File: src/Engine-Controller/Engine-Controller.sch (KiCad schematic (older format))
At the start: 14 parts, among them J1 Jumper_NO, U1 STM32H750VBTx

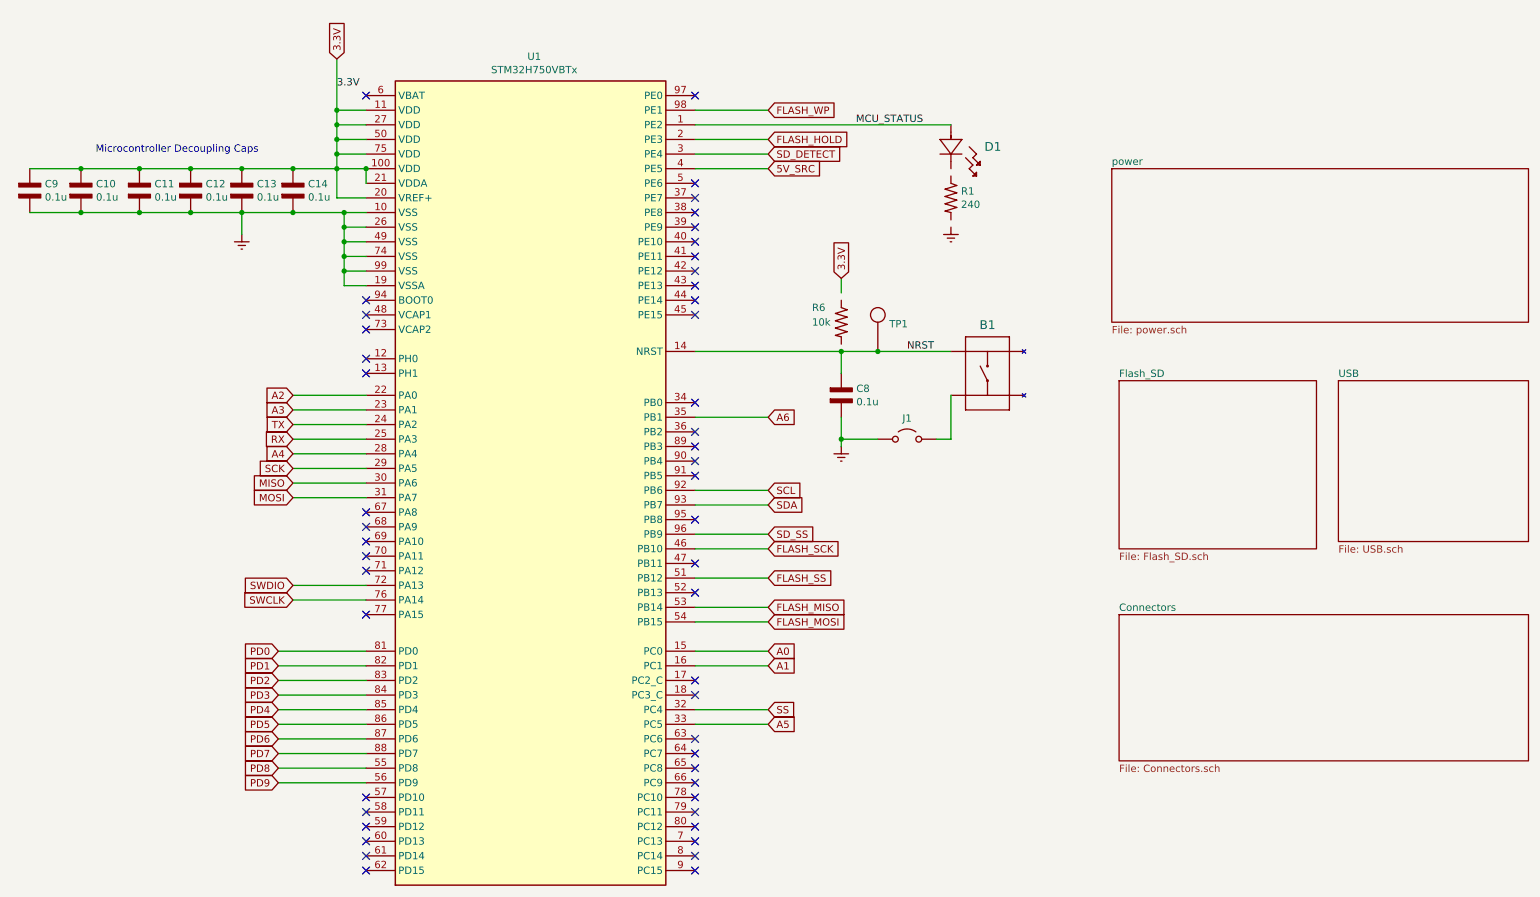
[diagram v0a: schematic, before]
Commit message: Added Ignition System to lib and schematic
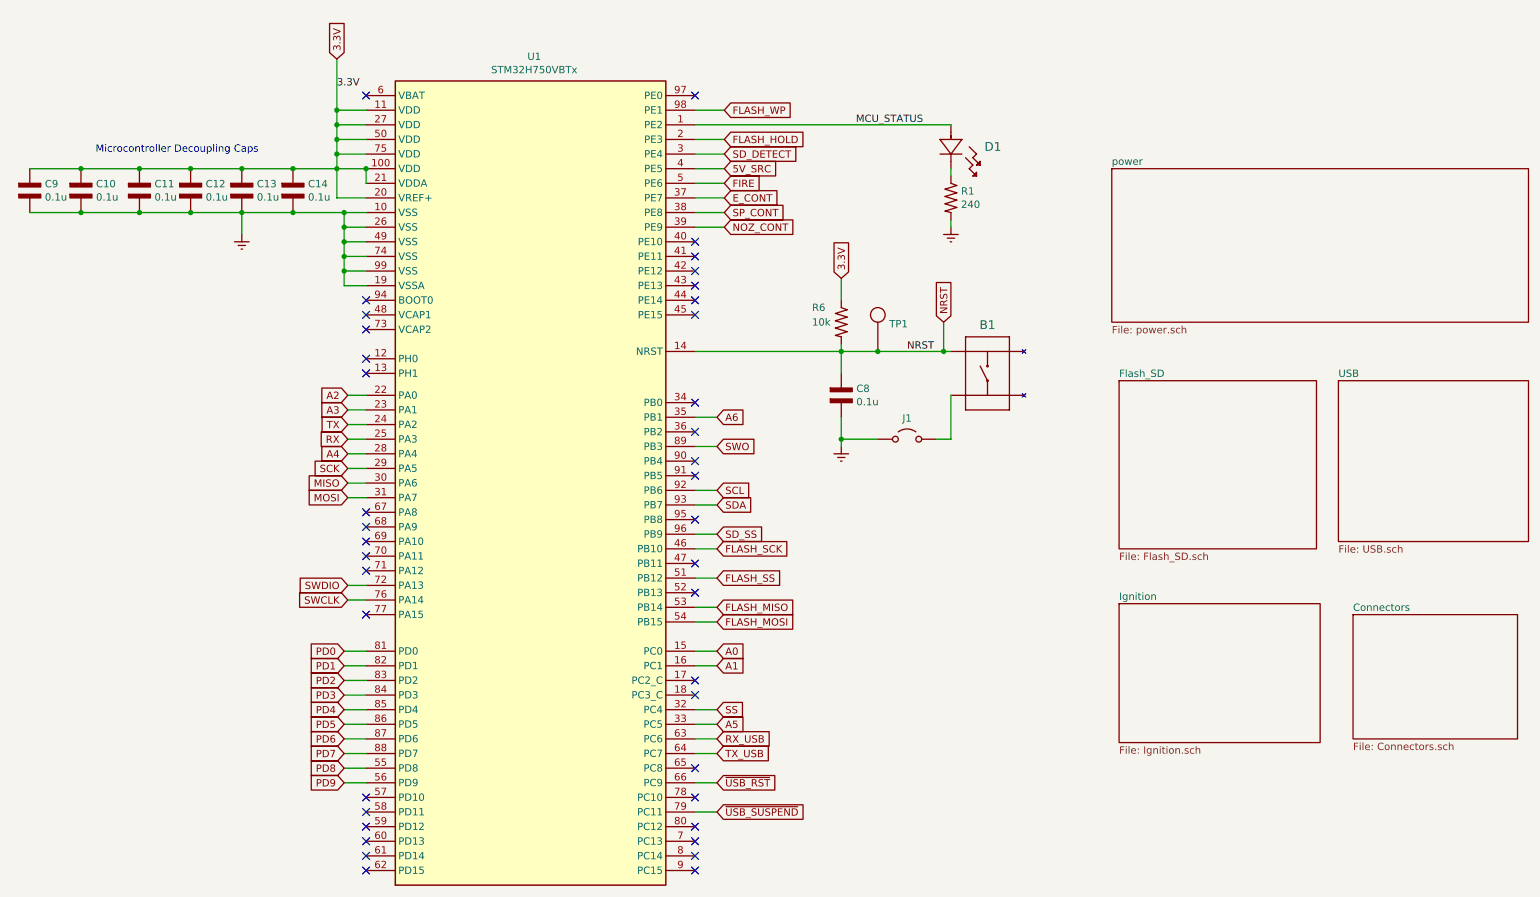
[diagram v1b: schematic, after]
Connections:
- net 3.3V: now also R6.1
- net Earth: now also R1.2
- net NRST: now also R6.2
- net at D1.1: now also R1.1
- net E_CONT: now reaches U1.37 (PE7)
- net SP_CONT: now reaches U1.38 (PE8)
- net NOZ_CONT: now reaches U1.39 (PE9)
- net FIRE: now reaches U1.5 (PE6)
- net RX_USB: now reaches U1.63 (PC6)
- net TX_USB: now reaches U1.64 (PC7)
- net ~USB_RST: now reaches U1.66 (PC9)
- net ~USB_SUSPEND: now reaches U1.79 (PC11)
- net SWO: now reaches U1.89 (PB3)
- no-connect marks 49 -> 40
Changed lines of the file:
@@
 $Descr A4 11693 8268
 encoding utf-8
-Sheet 1 5
+Sheet 1 6
 Title "Engine Controller Microcontroller Board"
 Date "2021-06-26"
@@
 $EndSheet
 $Sheet
-S 8150 4900 2800 1000
+S 9750 4900 1125 850
 U 60E24895
 F0 "Connectors" 50
 F1 "Connectors.sch" 50
 $EndSheet
-Text GLabel 2500 3700 0    50   Input ~ 0
+Text GLabel 2875 3700 0    50   Input ~ 0
 RX
-Text GLabel 2500 3600 0    50   Input ~ 0
+Text GLabel 2875 3600 0    50   Input ~ 0
 TX
 Text GLabel 2800 1100 1    50   Input ~ 0
@@
 	1    0    0    -1
 $EndComp
-Text GLabel 2400 5150 0    50   Input ~ 0
+Text GLabel 2850 5150 0    50   Input ~ 0
 PD0
-Text GLabel 2400 5250 0    50   Input ~ 0
+Text GLabel 2850 5250 0    50   Input ~ 0
 PD1
-Text GLabel 2400 5350 0    50   Input ~ 0
+Text GLabel 2850 5350 0    50   Input ~ 0
 PD2
-Text GLabel 2400 5450 0    50   Input ~ 0
+Text GLabel 2850 5450 0    50   Input ~ 0
 PD3
-Text GLabel 2400 5550 0    50   Input ~ 0
+Text GLabel 2850 5550 0    50   Input ~ 0
 PD4
-Text GLabel 2400 5650 0    50   Input ~ 0
+Text GLabel 2850 5650 0    50   Input ~ 0
 PD5
-Text GLabel 2400 5750 0    50   Input ~ 0
+Text GLabel 2850 5750 0    50   Input ~ 0
 PD6
-Text GLabel 2400 5850 0    50   Input ~ 0
+Text GLabel 2850 5850 0    50   Input ~ 0
 PD7
-Text GLabel 2400 5950 0    50   Input ~ 0
+Text GLabel 2850 5950 0    50   Input ~ 0
 PD8
-Text GLabel 2400 6050 0    50   Input ~ 0
+Text GLabel 2850 6050 0    50   Input ~ 0
 PD9
 Wire Wire Line
-	2400 5150 3000 5150
-Wire Wire Line
-	2400 5250 3000 5250
-Wire Wire Line
-	2400 5350 3000 5350
-Wire Wire Line
-	2400 5450 3000 5450
-Wire Wire Line
-	2400 5550 3000 5550
-Wire Wire Line
-	2400 5650 3000 5650
-Wire Wire Line
-	2400 5750 3000 5750
-Wire Wire Line
-	2400 5850 3000 5850
-Wire Wire Line
-	2400 5950 3000 5950
+	2850 5150 3000 5150
+Wire Wire Line
+	2850 5350 3000 5350
+Wire Wire Line
+	2850 5450 3000 5450
+Wire Wire Line
+	2850 5550 3000 5550
+Wire Wire Line
+	2850 5650 3000 5650
+Wire Wire Line
+	2850 5750 3000 5750
+Wire Wire Line
+	2850 5850 3000 5850
+Wire Wire Line
+	2850 5950 3000 5950
 Text Label 2800 1300 0    50   ~ 0
 3.3V
@@
 $EndComp
 Wire Wire Line
-	3000 3700 2500 3700
-Wire Wire Line
-	2500 3600 3000 3600
+	3000 3700 2875 3700
+Wire Wire Line
+	2875 3600 3000 3600
 $Comp
 L Engine-Controller:Earth #PWR0102
@@
 	1    0    0    -1
 $EndComp
-Wire Wire Line
-	6250 2700 6250 2600
 $Comp
 L Engine-Controller:RES_0603 R6
@@
 NRST
 Wire Wire Line
-	3000 6050 2400 6050
+	3000 6050 2850 6050
 $Comp
 L Engine-Controller:Jumper_NO J1
@@
 Wire Wire Line
 	6250 3250 6250 3100
-Text GLabel 5750 4850 2    50   Input ~ 0
+Text GLabel 5400 4850 2    50   Input ~ 0
 FLASH_MISO
 Wire Wire Line
-	5750 4850 5250 4850
-Text GLabel 5750 4950 2    50   Input ~ 0
+	5400 4850 5250 4850
+Text GLabel 5400 4950 2    50   Input ~ 0
 FLASH_MOSI
 Wire Wire Line
-	5750 4950 5250 4950
+	5400 4950 5250 4950
 $Sheet
 S 8150 3300 1350 1150
@@
 Connection ~ 6500 3100
 Wire Wire Line
-	6500 3100 7000 3100
-Text GLabel 2500 3800 0    50   Input ~ 0
+	6500 3100 6950 3100
+Text GLabel 2875 3800 0    50   Input ~ 0
 A4
-Text GLabel 5750 5650 2    50   Input ~ 0
+Text GLabel 5400 5650 2    50   Input ~ 0
 A5
 Wire Wire Line
-	2500 3800 3000 3800
-Wire Wire Line
-	5750 5650 5250 5650
-Text GLabel 5750 1450 2    50   Input ~ 0
+	2875 3800 3000 3800
+Wire Wire Line
+	5400 5650 5250 5650
+Text GLabel 5450 1450 2    50   Input ~ 0
 FLASH_WP
-Text GLabel 5750 1650 2    50   Input ~ 0
+Text GLabel 5450 1650 2    50   Input ~ 0
 FLASH_HOLD
-Text GLabel 5750 1750 2    50   Input ~ 0
+Text GLabel 5450 1750 2    50   Input ~ 0
 SD_DETECT
 Text GLabel 6250 2600 1    50   Input ~ 0
 3.3V
-Text GLabel 5750 1850 2    50   Input ~ 0
+Text GLabel 5450 1850 2    50   Input ~ 0
 5V_SRC
 Wire Wire Line
 	3000 1950 3000 1850
-Connection ~ 3000 1850
 Wire Wire Line
 	5250 3100 6250 3100
@@
 	2800 1450 3000 1450
 Wire Wire Line
-	5250 3550 5750 3550
-Wire Wire Line
-	3000 3500 2500 3500
-Wire Wire Line
-	3000 3400 2500 3400
-Wire Wire Line
-	5250 5250 5750 5250
-Wire Wire Line
-	5250 5150 5750 5150
-Wire Wire Line
-	5250 4350 5750 4350
-Text GLabel 5750 4350 2    50   Input ~ 0
+	5250 3550 5400 3550
+Wire Wire Line
+	3000 3500 2875 3500
+Wire Wire Line
+	3000 3400 2875 3400
+Wire Wire Line
+	5250 5150 5400 5150
+Wire Wire Line
+	5250 4350 5400 4350
+Text GLabel 5400 4350 2    50   Input ~ 0
 SD_SS
-Text GLabel 5750 3550 2    50   Input ~ 0
+Text GLabel 5400 3550 2    50   Input ~ 0
 A6
-Text GLabel 2500 3500 0    50   Input ~ 0
+Text GLabel 2875 3500 0    50   Input ~ 0
 A3
-Text GLabel 2500 3400 0    50   Input ~ 0
+Text GLabel 2875 3400 0    50   Input ~ 0
 A2
-Text GLabel 5750 5250 2    50   Input ~ 0
+Text GLabel 5400 5250 2    50   Input ~ 0
 A1
-Text GLabel 5750 5150 2    50   Input ~ 0
+Text GLabel 5400 5150 2    50   Input ~ 0
 A0
 Wire Wire Line
-	5250 4650 5750 4650
-Text GLabel 5750 4650 2    50   Input ~ 0
+	5250 4650 5400 4650
+Text GLabel 5400 4650 2    50   Input ~ 0
 FLASH_SS
 Wire Wire Line
-	5250 4450 5750 4450
-Text GLabel 5750 4450 2    50   Input ~ 0
+	5250 4450 5400 4450
+Text GLabel 5400 4450 2    50   Input ~ 0
 FLASH_SCK
 Wire Wire Line
-	3000 4800 2500 4800
-Wire Wire Line
-	3000 4700 2500 4700
-Text GLabel 2500 4700 0    50   Input ~ 0
+	3000 4800 2875 4800
+Wire Wire Line
+	3000 4700 2875 4700
+Text GLabel 2875 4700 0    50   Input ~ 0
 SWDIO
-Text GLabel 2500 4800 0    50   Input ~ 0
+Text GLabel 2875 4800 0    50   Input ~ 0
 SWCLK
 Wire Wire Line
-	5250 4150 5750 4150
-Wire Wire Line
-	5750 4050 5250 4050
-Wire Wire Line
-	5750 5550 5250 5550
-Wire Wire Line
-	2500 3900 3000 3900
-Wire Wire Line
-	3000 4100 2500 4100
-Wire Wire Line
-	3000 4000 2500 4000
-Text GLabel 5750 5550 2    50   Input ~ 0
+	5250 4150 5400 4150
+Wire Wire Line
+	5400 4050 5250 4050
+Wire Wire Line
+	5400 5550 5250 5550
+Wire Wire Line
+	2875 3900 3000 3900
+Wire Wire Line
+	3000 4100 2875 4100
+Wire Wire Line
+	3000 4000 2875 4000
+Text GLabel 5400 5550 2    50   Input ~ 0
 SS
-Text GLabel 5750 4050 2    50   Input ~ 0
+Text GLabel 5400 4050 2    50   Input ~ 0
 SCL
-Text GLabel 5750 4150 2    50   Input ~ 0
+Text GLabel 5400 4150 2    50   Input ~ 0
 SDA
-Text GLabel 2500 3900 0    50   Input ~ 0
+Text GLabel 2875 3900 0    50   Input ~ 0
 SCK
-Text GLabel 2500 4000 0    50   Input ~ 0
+Text GLabel 2875 4000 0    50   Input ~ 0
 MISO
-Text GLabel 2500 4100 0    50   Input ~ 0
+Text GLabel 2875 4100 0    50   Input ~ 0
 MOSI
 $Comp
@@
 	2800 2050 2800 1850
 Wire Wire Line
-	5250 1450 5750 1450
-Wire Wire Line
-	5250 1650 5750 1650
-Wire Wire Line
-	5250 1750 5750 1750
-Wire Wire Line
-	5250 1850 5750 1850
+	5250 1450 5450 1450
+Wire Wire Line
+	5250 1650 5450 1650
+Wire Wire Line
+	5250 1750 5450 1750
+Wire Wire Line
+	5250 1850 5450 1850
 Wire Wire Line
 	3000 2650 2850 2650
@@
 	2850 2650 2850 2550
 Connection ~ 2850 2550
-$Comp
-L Engine-Controller:STM32H750VBTx U1
-U 1 1 614B51F2
-P 4150 4150
-F 0 "U1" H 4150 7217 50  0000 C CNN
-F 1 "STM32H750VBTx" H 4150 7126 50  0000 C CNN
-F 2 "Engine-Controller:STM32H750VBT6" H 3450 1550 50  0001 R CNN
-F 3 "https://www.st.com/resource/en/datasheet/stm32h750ib.pdf" H 4150 4150 50  0001 C CNN
-	1    4150 4150
-	1    0    0    -1
-$EndComp
 NoConn ~ 3000 1350
 NoConn ~ 3000 2750
@@
 NoConn ~ 3000 4500
 NoConn ~ 3000 4600
-NoConn ~ 3000 4900
 NoConn ~ 3000 6150
 NoConn ~ 3000 6250
@@
 NoConn ~ 5250 6450
 NoConn ~ 5250 6350
-NoConn ~ 5250 6250
 NoConn ~ 5250 6150
-NoConn ~ 5250 6050
-NoConn ~ 5250 5950
-NoConn ~ 5250 5850
-NoConn ~ 5250 5750
 NoConn ~ 5250 5450
 NoConn ~ 5250 5350
@@
 NoConn ~ 5250 4250
 NoConn ~ 5250 3950
-NoConn ~ 5250 3850
-NoConn ~ 5250 3750
 NoConn ~ 5250 3650
 NoConn ~ 5250 3450
@@
 NoConn ~ 5250 2450
 NoConn ~ 5250 2350
-NoConn ~ 5250 2250
-NoConn ~ 5250 2150
-NoConn ~ 5250 2050
-NoConn ~ 5250 1950
 NoConn ~ 5250 1350
 Wire Wire Line
 	5250 1550 7000 1550
+Text GLabel 5400 5750 2    50   Input ~ 0
+RX_USB
+Wire Wire Line
+	5250 5750 5400 5750
+Text GLabel 5400 5850 2    50   Input ~ 0
+TX_USB
+Wire Wire Line
+	5250 5850 5400 5850
+Text GLabel 5400 6050 2    50   Input ~ 0
+~USB_RST
+Wire Wire Line
+	5250 6050 5400 6050
+NoConn ~ 5250 5950
+Text GLabel 5400 6250 2    50   Input ~ 0
+~USB_SUSPEND
+Wire Wire Line
+	5250 6250 5400 6250
+Text GLabel 6950 2900 1    50   Input ~ 0
+NRST
+Connection ~ 6950 3100
+Wire Wire Line
+	6950 3100 7000 3100
+Text GLabel 5400 3750 2    50   Input ~ 0
+SWO
+Wire Wire Line
+	5250 3750 5400 3750
+Connection ~ 3000 1850
+Wire Wire Line
+	6950 2900 6950 3100
+Wire Wire Line
+	5250 5250 5400 5250
+Wire Wire Line
+	2850 5250 3000 5250
+$Comp
+L Engine-Controller:STM32H750VBTx U1
+U 1 1 614B51F2
+P 4150 4150
+F 0 "U1" H 4150 7217 50  0000 C CNN
+F 1 "STM32H750VBTx" H 4150 7126 50  0000 C CNN
+F 2 "Engine-Controller:STM32H750VBT6" H 3450 1550 50  0001 R CNN
+F 3 "https://www.st.com/resource/en/datasheet/stm32h750ib.pdf" H 4150 4150 50  0001 C CNN
+	1    4150 4150
+	1    0    0    -1
+$EndComp
+$Sheet
+S 8150 4825 1375 950
+U 618AD610
+F0 "Ignition" 50
+F1 "Ignition.sch" 50
+$EndSheet
+NoConn ~ 5250 3850
+NoConn ~ 3000 4900
+Wire Wire Line
+	6250 2600 6250 2750
+Wire Wire Line
+	6250 3100 6250 3050
+Wire Wire Line
+	7000 1900 7000 1850
+Wire Wire Line
+	7000 2250 7000 2200
+Text GLabel 5450 1950 2    50   Input ~ 0
+FIRE
+Wire Wire Line
+	5250 1950 5450 1950
+Text GLabel 5450 2050 2    50   Input ~ 0
+E_CONT
+Wire Wire Line
+	5450 2050 5250 2050
+Text GLabel 5450 2150 2    50   Input ~ 0
+SP_CONT
+Text GLabel 5450 2250 2    50   Input ~ 0
+NOZ_CONT
+Wire Wire Line
+	5250 2150 5450 2150
+Wire Wire Line
+	5250 2250 5450 2250
 $EndSCHEMATC

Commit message: Add Internal regulator stability caps
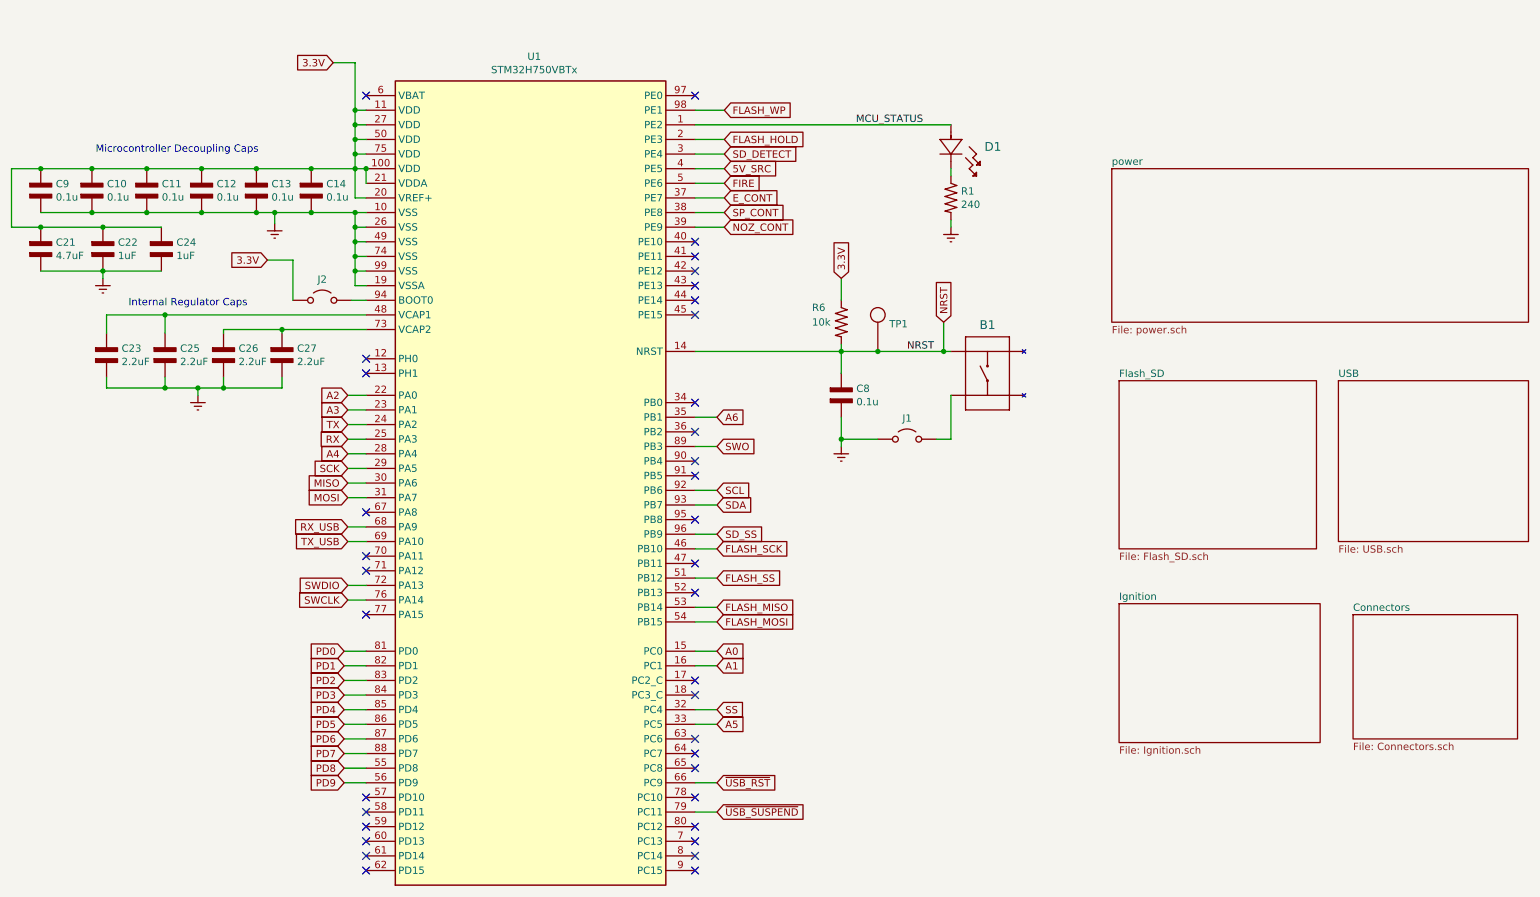
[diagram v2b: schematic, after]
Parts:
- added C21: 4.7uF, Engine-Controller:CAP_0603, symbol Engine-Controller:CAP_0603
- added C22, C24: 1uF, Engine-Controller:CAP_0603, symbol Engine-Controller:CAP_0603
- added C23, C25, C26, C27: 2.2uF, Engine-Controller:CAP_0603, symbol Engine-Controller:CAP_0603
- added J2: Jumper_NO, Engine-Controller:Jumper-NO, symbol Engine-Controller:Jumper_NO
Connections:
- net 3.3V: now also C21.2, C22.2, C24.2, J2.1 (A)
- net Earth: now also C21.1, C22.1, C23.1, C24.1, C25.1, C26.1, C27.1
- net RX_USB: now also U1.68 (PA9); no longer U1.63 (PC6)
- net TX_USB: now also U1.69 (PA10); no longer U1.64 (PC7)
- net at U1.48 (VCAP1): now also C23.2, C25.2
- net at U1.73 (VCAP2): now also C26.2, C27.2
- net at U1.94 (BOOT0): now also J2.2 (B)
- no-connect marks 40 -> 37
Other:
- note added: "Internal Regulator Caps"
- moved on the sheet: C10, C11, C12, C13, C14, C9

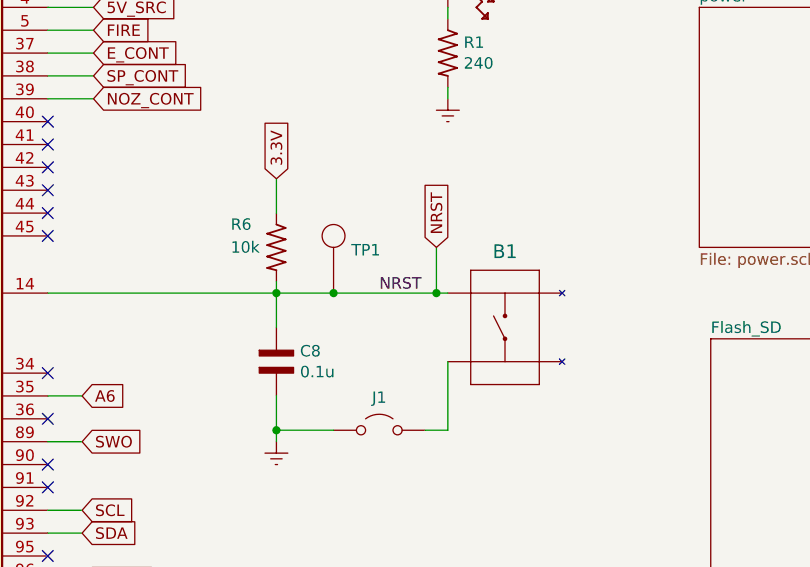
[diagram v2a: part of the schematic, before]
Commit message: Updated Buffer Symbol
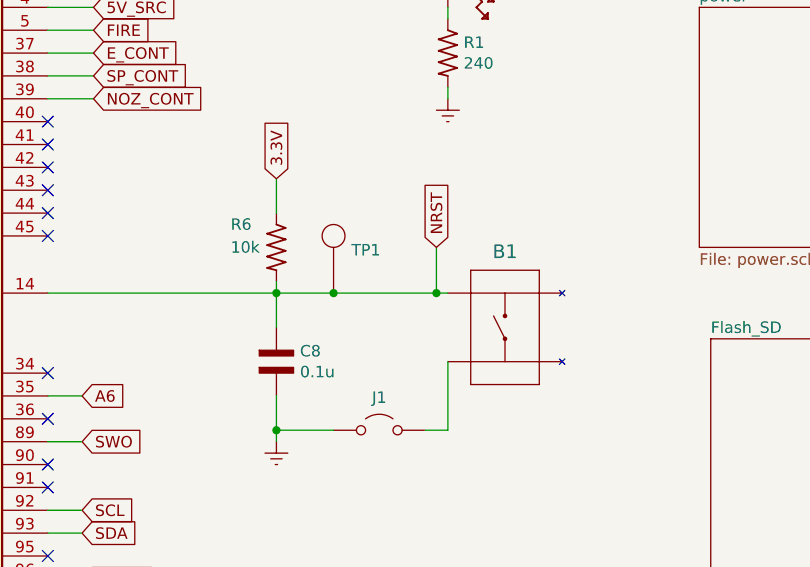
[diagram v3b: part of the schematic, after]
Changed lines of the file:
@@
 Text Notes 1150 1750 0    50   ~ 0
 Microcontroller Decoupling Caps
-Text Label 6700 3100 0    50   ~ 0
-NRST
 Wire Wire Line
 	3000 6050 2850 6050
